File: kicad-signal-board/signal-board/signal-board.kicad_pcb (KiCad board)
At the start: 2 copper layers, 83.6 x 61 mm, 35 parts, among them IC1 74HCT245, J1 Conn_02x09_Odd_Even, J2 Conn_02x08_Odd_Even, J3 5V Pwr Conn, J4 24V Screw Term, SW1 SW_MEC_5G, SW2 SW_MEC_5G, U1 ESP32-DEVKITC-32D, U2 MC33063AD

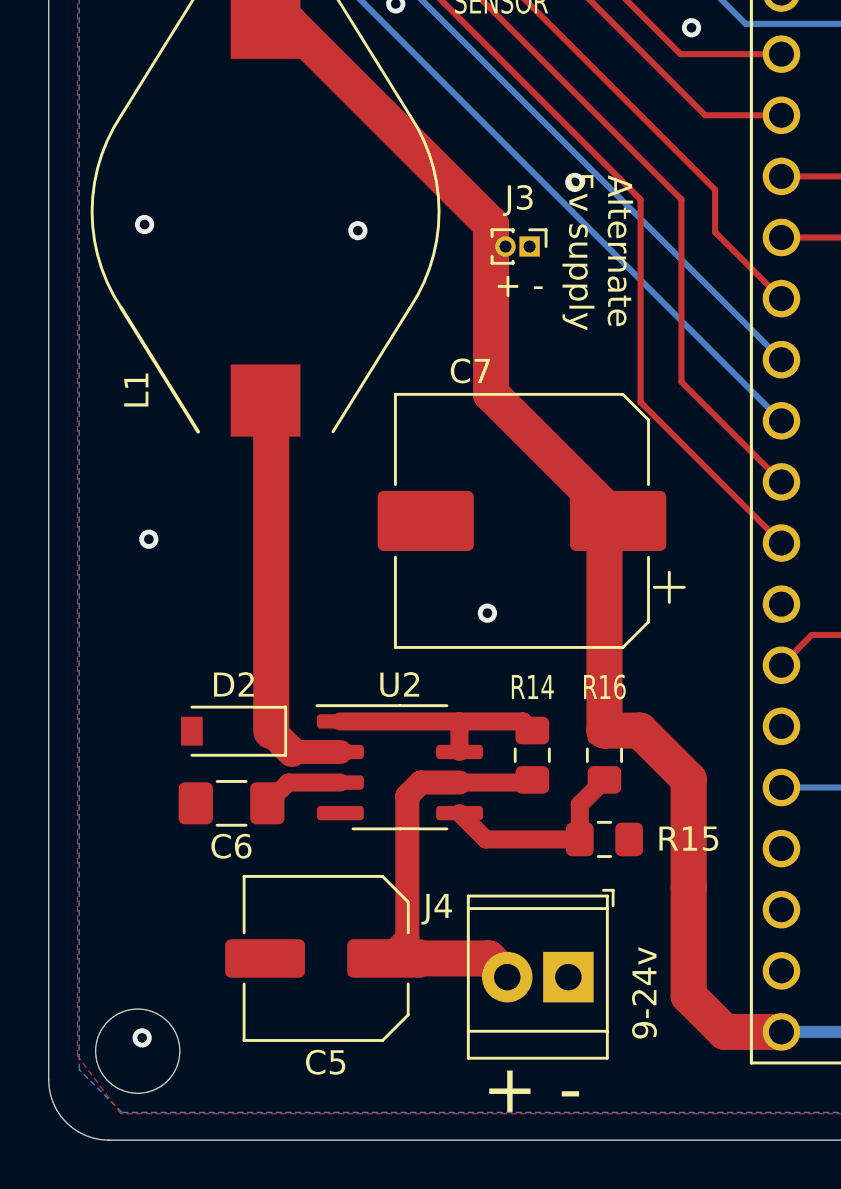
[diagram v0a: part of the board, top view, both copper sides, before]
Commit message: Fixed DRC check error with alternate 5V supply footprint using 2.54mm instead of 1.0mm 1x2 header
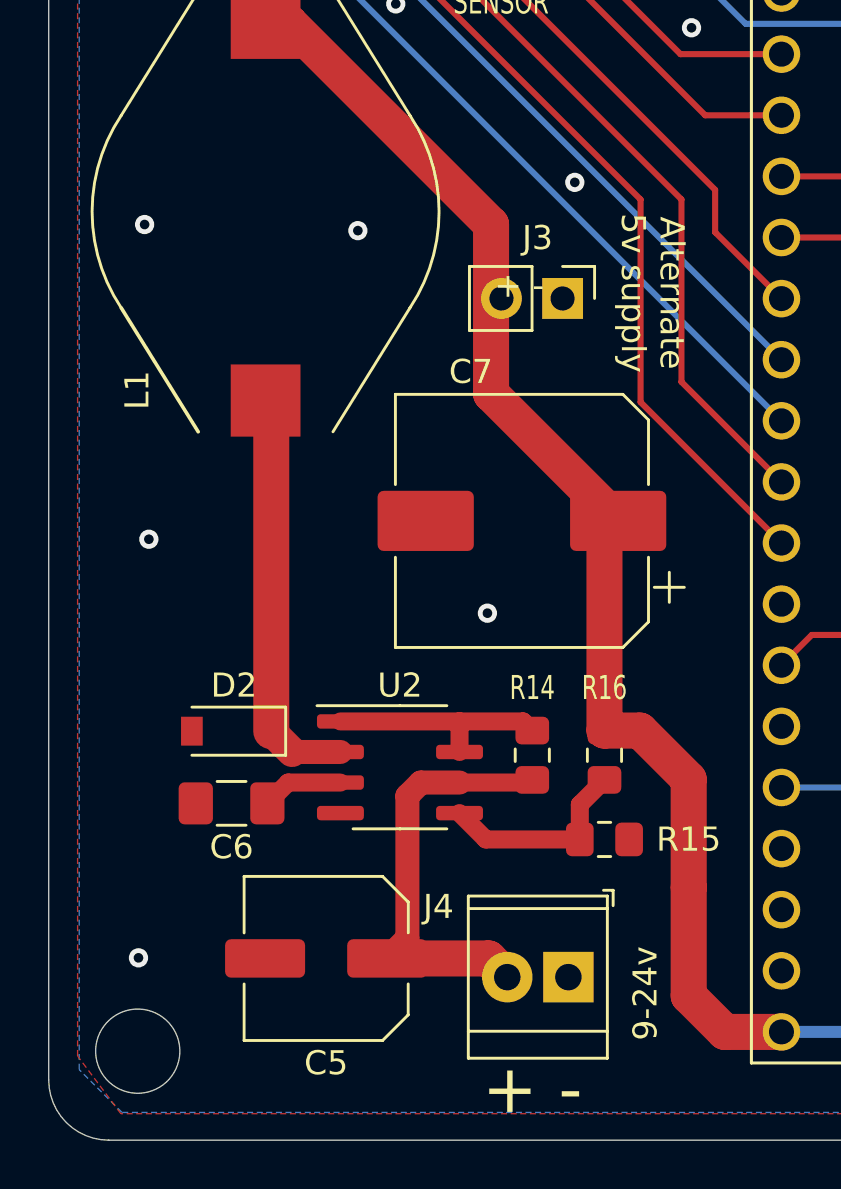
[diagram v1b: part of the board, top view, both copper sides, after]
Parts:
- J3: footprint Connector_PinHeader_1.00mm:PinHeader_1x02_P1.00mm_Vertical -> Connector_PinHeader_2.54mm:PinHeader_1x02_P2.54mm_Vertical
- R16: value 3.8K -> 3.6K
- moved J3 2.56 mm to (113.3, 75.5)
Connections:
- net +24V renamed 7V_to_24V_Input
